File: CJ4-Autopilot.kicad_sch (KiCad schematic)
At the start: 39 parts, among them J1 CRS encoder, J2 FLC encoder, J3 HDG encoder, J4 ALT encoder, J5 CRS encoder, SW1 FD1, SW10 ALT, SW11 YD, SW12 XFR, SW13 AP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

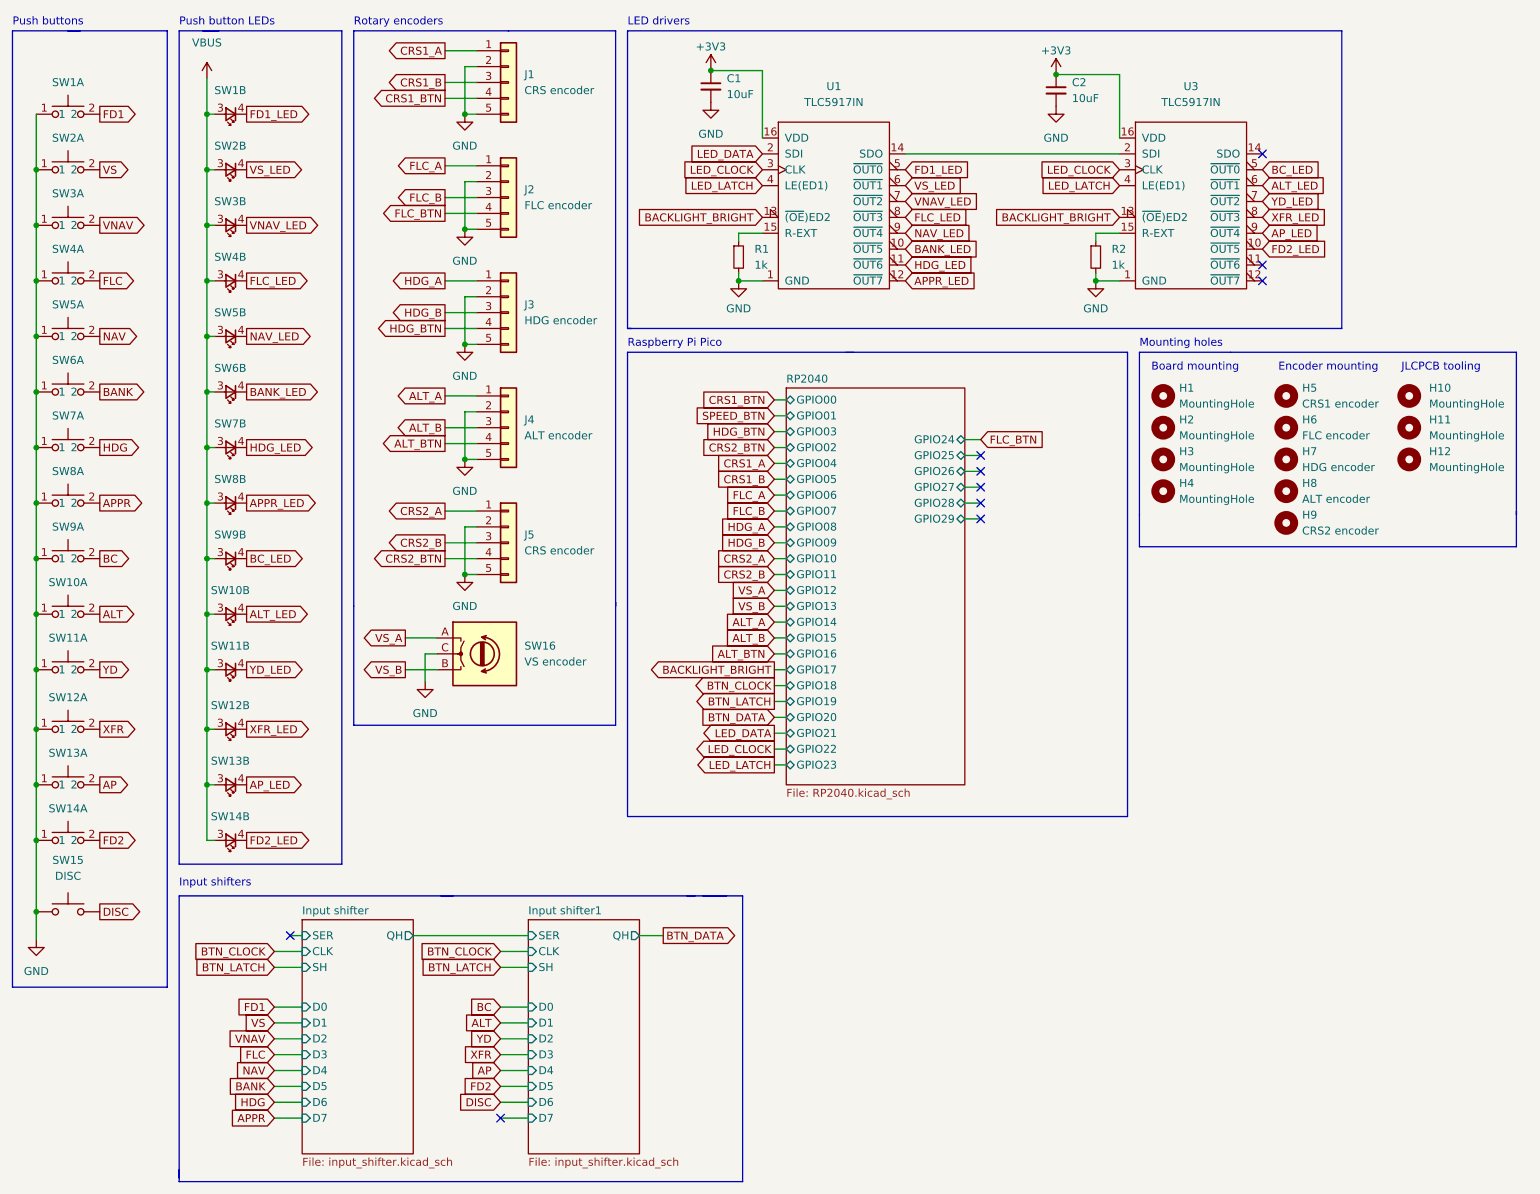
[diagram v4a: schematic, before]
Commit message: Moved chips, rotated encoder. Lots of traces, it's gonna work!
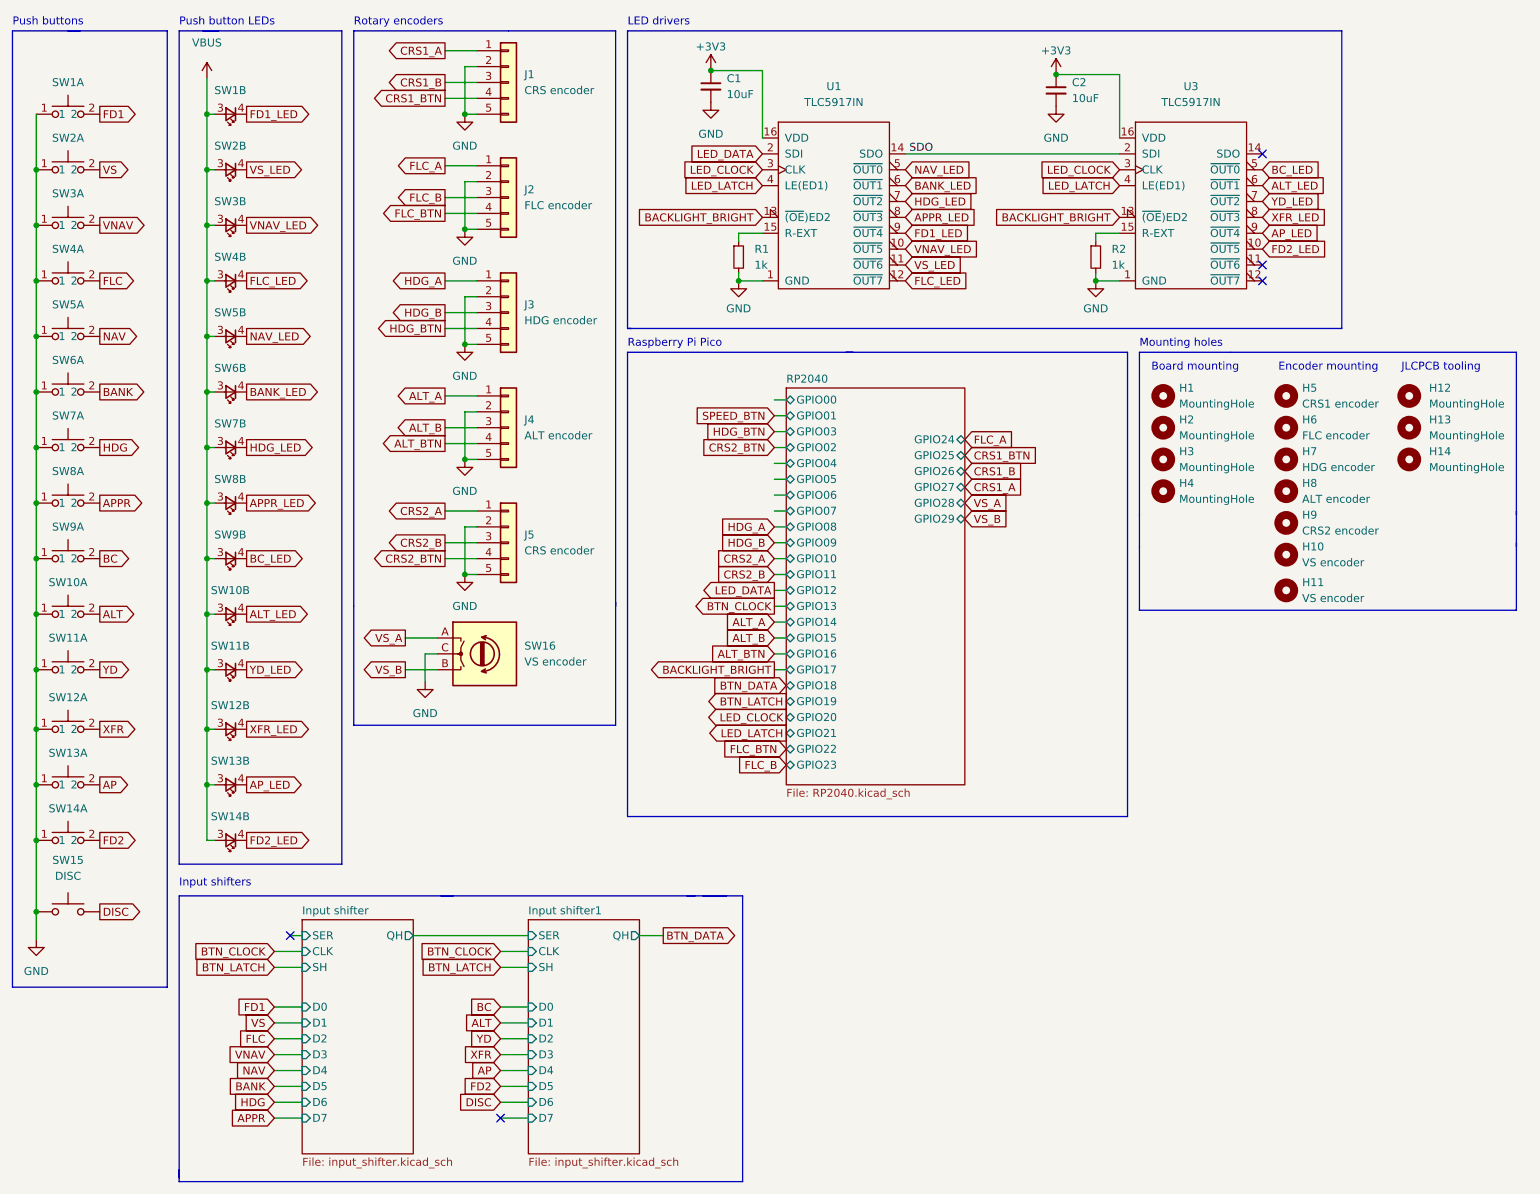
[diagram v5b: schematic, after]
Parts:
- added H10, H11: VS encoder, MountingHole:MountingHole_3.2mm_M3, symbol Mechanical:MountingHole
- renumbered H10 to H12, H11 to H13, H12 to H14
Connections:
- net APPR_LED: now also U1.8 (~{OUT3}); no longer U1.12 (~{OUT7})
- net BANK_LED: now also U1.6 (~{OUT1}); no longer U1.10 (~{OUT5})
- net FD1_LED: now also U1.9 (~{OUT4}); no longer U1.5 (~{OUT0})
- net FLC_LED: now also U1.12 (~{OUT7}); no longer U1.8 (~{OUT3})
- net HDG_LED: now also U1.7 (~{OUT2}); no longer U1.11 (~{OUT6})
- net NAV_LED: now also U1.5 (~{OUT0}); no longer U1.9 (~{OUT4})
- net VNAV_LED: now also U1.10 (~{OUT5}); no longer U1.7 (~{OUT2})
- net VS_LED: now also U1.11 (~{OUT6}); no longer U1.6 (~{OUT1})
- net SDO: now reaches U1.14 (SDO), U3.2 (SDI)
- no-connect marks 10 -> 5

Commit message: Left side fully connected
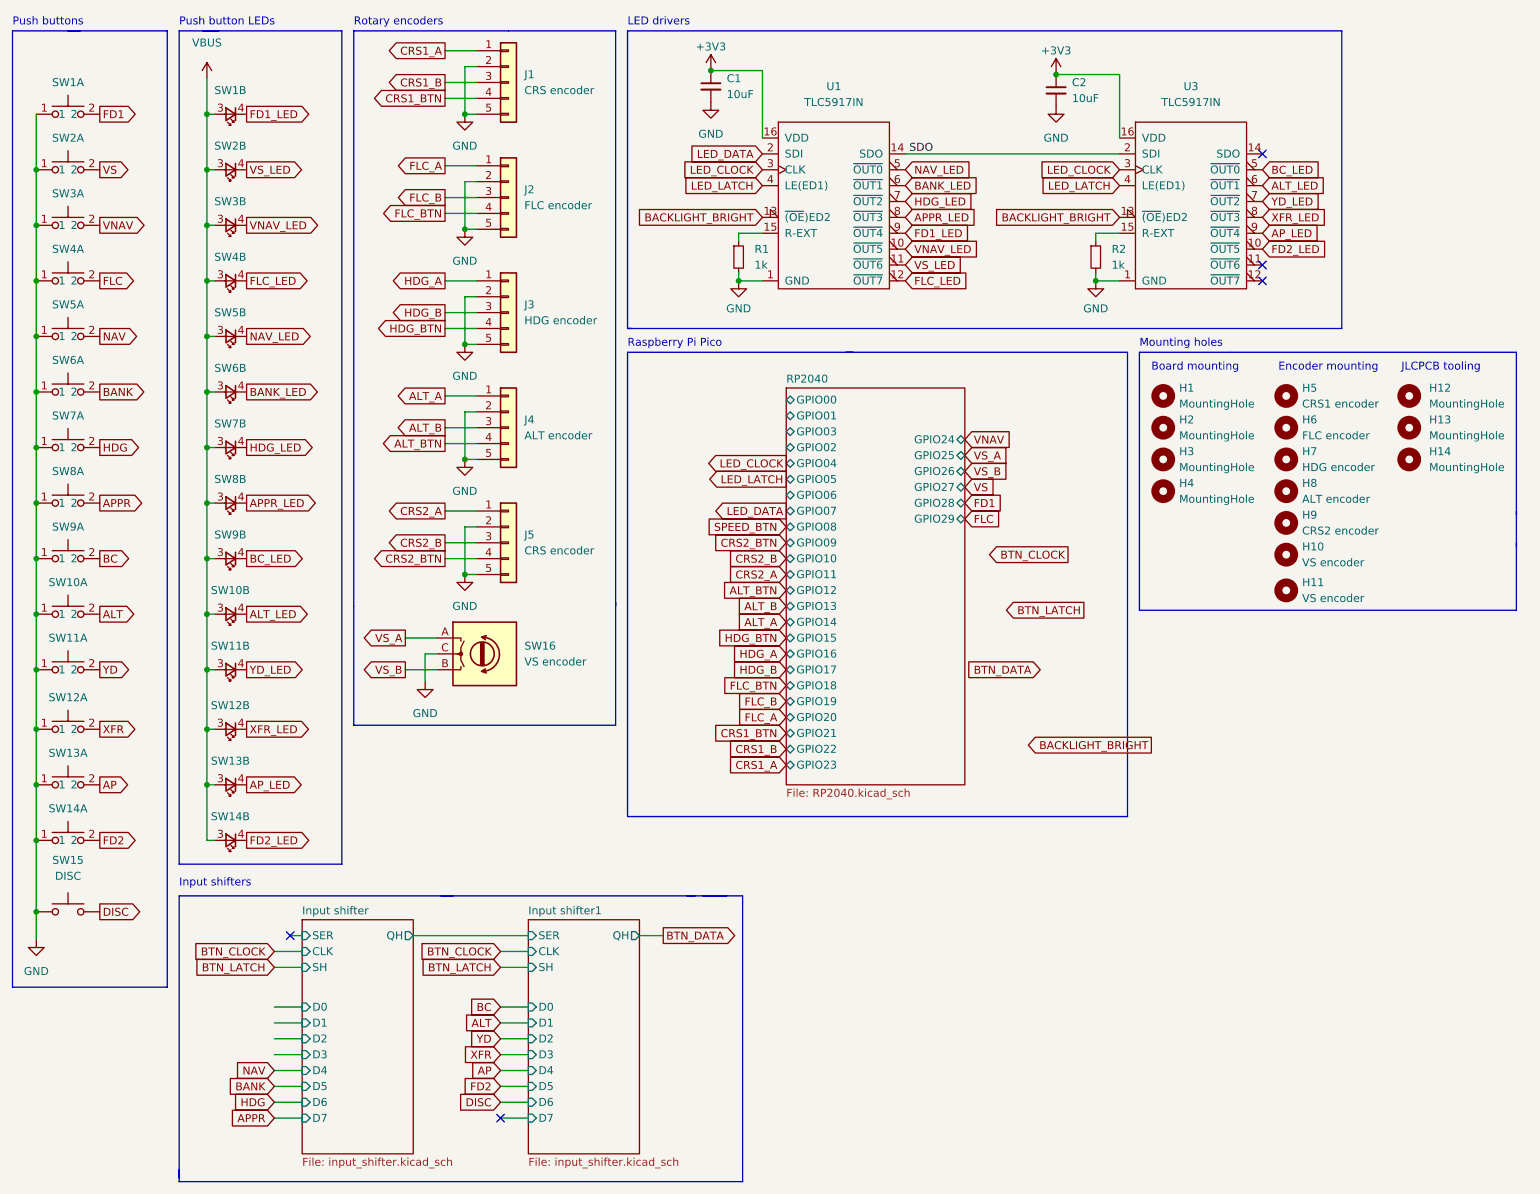
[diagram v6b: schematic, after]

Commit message: Tons and tons of traces
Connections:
- net ALT_LED: now also U3.8 (~{OUT3}); no longer U3.6 (~{OUT1})
- net APPR_LED: now also U3.7 (~{OUT2}); no longer U1.8 (~{OUT3})
- net AP_LED: now also U3.11 (~{OUT6}); no longer U3.9 (~{OUT4})
- net BANK_LED: now also U1.9 (~{OUT4}); no longer U1.6 (~{OUT1})
- net BC_LED: now also U3.6 (~{OUT1}); no longer U3.5 (~{OUT0})
- net FD1_LED: now also U1.5 (~{OUT0}); no longer U1.9 (~{OUT4})
- net FLC_LED: now also U1.8 (~{OUT3}); no longer U1.12 (~{OUT7})
- net HDG_LED: now also U1.11 (~{OUT6}); no longer U1.7 (~{OUT2})
- net NAV_LED: now also U1.10 (~{OUT5}); no longer U1.5 (~{OUT0})
- net VNAV_LED: now also U1.6 (~{OUT1}); no longer U1.10 (~{OUT5})
- net VS_LED: now also U1.7 (~{OUT2}); no longer U1.11 (~{OUT6})
- net XFR_LED: now also U3.5 (~{OUT0}); no longer U3.8 (~{OUT3})
- net YD_LED: now also U3.9 (~{OUT4}); no longer U3.7 (~{OUT2})
- no-connect marks 5 -> 7

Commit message: Fully routed!
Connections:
- net FD2_LED: now also U3.9 (~{OUT4}); no longer U3.10 (~{OUT5})
- net YD_LED: now also U3.10 (~{OUT5}); no longer U3.9 (~{OUT4})
- no-connect marks 7 -> 11
